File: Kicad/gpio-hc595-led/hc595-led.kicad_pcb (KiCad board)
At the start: 2 copper layers, 50 x 25 mm, 14 parts, among them K1 GPIO IN, K2 GPIO OUT, K3 DATA OUT, U1 74HC595, U2 3M-SJ5376

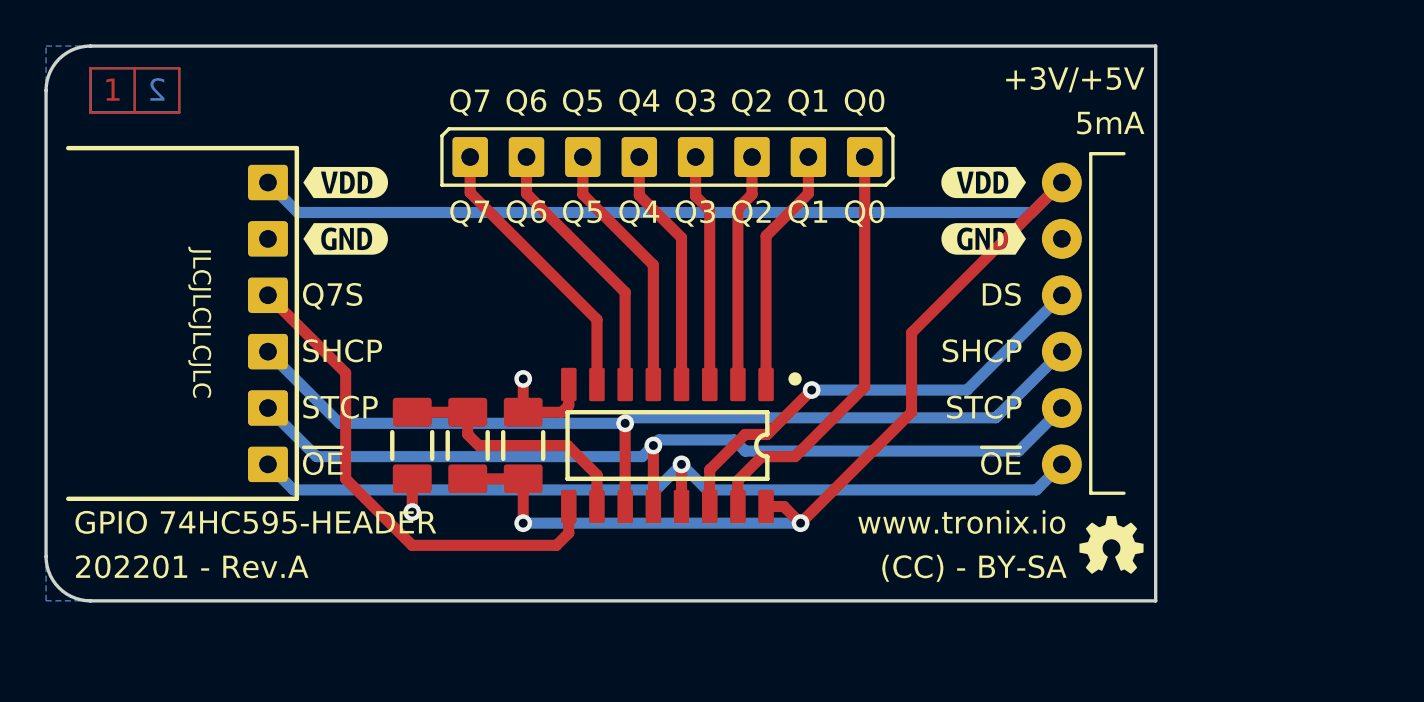
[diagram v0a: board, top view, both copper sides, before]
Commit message: GPIO HC595
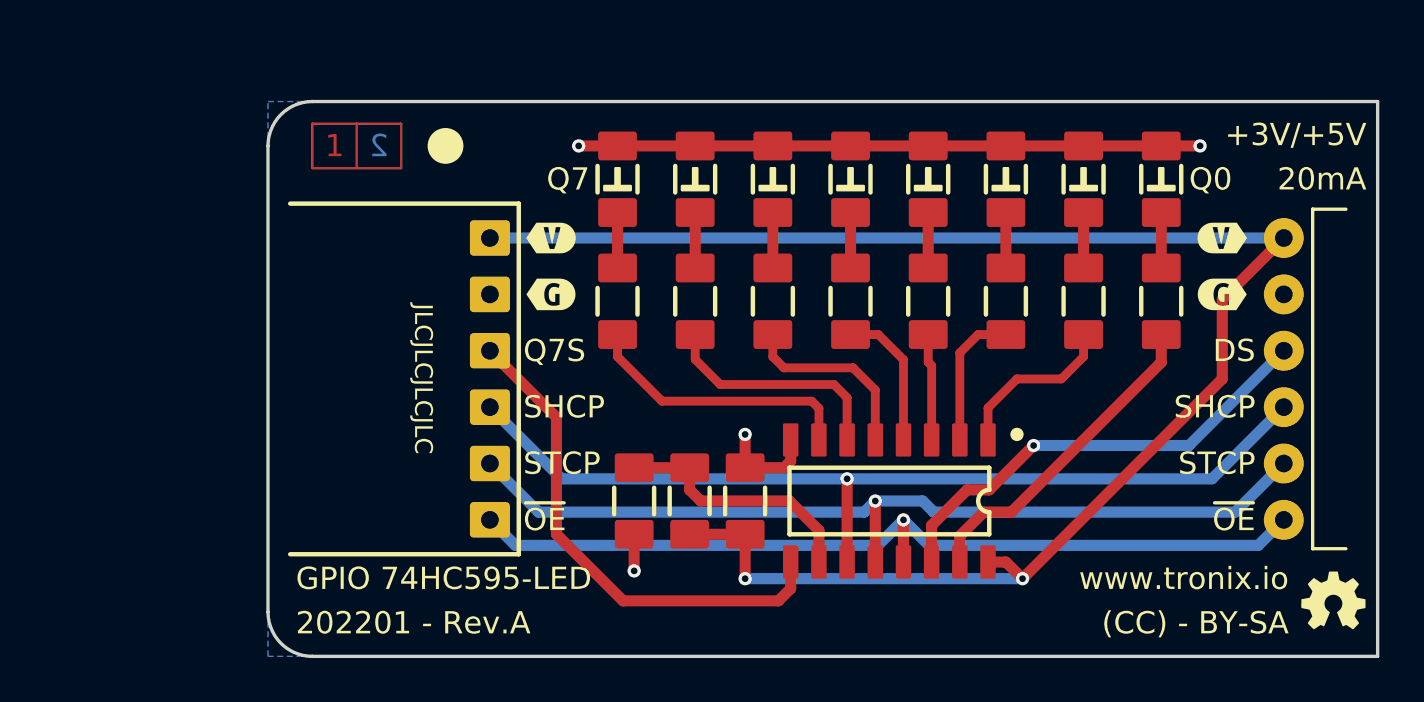
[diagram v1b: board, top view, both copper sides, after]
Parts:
- removed the C2 at (136.5, 90.5)
- removed K3: DATA OUT, tronixio:HARWIN-M20-999084x
- removed kibuzzard-62B2FE1A: G***, kibuzzard-62B2FE1A
- removed kibuzzard-62B2FE4D: G***, kibuzzard-62B2FE4D
- removed kibuzzard-62EAC0B7: G***, kibuzzard-62EAC0B7
- removed kibuzzard-62EAC0C0: G***, kibuzzard-62EAC0C0
- added C1: 10n, tronixio:CAPACITOR-SMD-1206, F.Cu at (141.5, 93.0)
- added LED1: D0, tronixio:LED-SMD-1206, F.Cu at (165.2, 78.5)
- added LED2: D1, tronixio:LED-SMD-1206, F.Cu at (161.8, 78.5)
- added LED3: D2, tronixio:LED-SMD-1206, F.Cu at (158.2, 78.5)
- added LED4: D3, tronixio:LED-SMD-1206, F.Cu at (154.8, 78.5)
- added LED5: D4, tronixio:LED-SMD-1206, F.Cu at (151.2, 78.5)
- added LED6: D5, tronixio:LED-SMD-1206, F.Cu at (147.8, 78.5)
- added LED7: D6, tronixio:LED-SMD-1206, F.Cu at (144.2, 78.5)
- added LED8: D7, tronixio:LED-SMD-1206, F.Cu at (140.8, 78.5)
- added R2: 4k7, tronixio:RESISTOR-SMD-1206, F.Cu at (140.8, 84.0)
- added R3: 4k7, tronixio:RESISTOR-SMD-1206, F.Cu at (144.2, 84.0)
- added R4: 4k7, tronixio:RESISTOR-SMD-1206, F.Cu at (147.8, 84.0)
- added R5: 4k7, tronixio:RESISTOR-SMD-1206, F.Cu at (151.2, 84.0)
- added R6: 4k7, tronixio:RESISTOR-SMD-1206, F.Cu at (154.8, 84.0)
- added R7: 4k7, tronixio:RESISTOR-SMD-1206, F.Cu at (158.2, 84.0)
- added R8: 4k7, tronixio:RESISTOR-SMD-1206, F.Cu at (161.8, 84.0)
- added R9: 4k7, tronixio:RESISTOR-SMD-1206, F.Cu at (165.2, 84.0)
- added kibuzzard-62B79DF9: G***, kibuzzard-62B79DF9, F.Cu at (137.8, 81.2)
- added kibuzzard-62B79E59: G***, kibuzzard-62B79E59, F.Cu at (137.8, 83.7)
- added kibuzzard-62B79EB2: G***, kibuzzard-62B79EB2, F.Cu at (168.0, 81.2)
- added kibuzzard-62B79EC3: G***, kibuzzard-62B79EC3, F.Cu at (168.0, 83.7)
- C2: renamed from C1; value 10n -> 100n
- R1: value 10K -> 10k
- moved C2 15.2 mm to (146.5, 93.0), turned to 90 degrees
- moved G*** 10.3 mm to (173.0, 97.5)
- moved K1 10.3 mm to (170.8, 81.2)
- moved K2 10.3 mm to (135.0, 93.8)
- moved R1 10.3 mm to (144.0, 93.0)
- moved U1 10.3 mm to (153.0, 93.0)
- moved U2 10.3 mm to (141.5, 87.5)
- moved GT 10.0 mm to (157.0, 81.5)
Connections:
- net POWER-GND renamed GND
- C2 pad 1: Net-(U1-~{MR}) -> +VDD
- K1 pad 1: POWER-VBAT -> +VDD
- K2 pad 6: POWER-VBAT -> +VDD
- R1 pad 1: POWER-VBAT -> +VDD
- U1 pad 16: POWER-VBAT -> +VDD
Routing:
- net POWER-VBAT: track 76.0 -> 0.00 mm, vias 2 -> 0
- net +VDD: track 0.00 -> 74.9 mm, vias 0 -> 2
- net GND: track 6.13 -> 34.3 mm, vias 2 -> 4
- net Net-(U1-Q3): track 10.5 -> 4.81 mm
- net Net-(U1-Q4): track 11.0 -> 6.47 mm
- net Net-(U1-Q0): track 19.0 -> 14.7 mm
- net Net-(U1-Q2): track 10.5 -> 6.34 mm
- net Net-(U1-Q1): track 11.0 -> 7.70 mm
- net Net-(U1-Q5): track 11.6 -> 8.49 mm
- net Net-(LED8-A): track 0.00 -> 2.50 mm
- net Net-(LED7-A): track 0.00 -> 2.50 mm
- net Net-(LED6-A): track 0.00 -> 2.50 mm
- net Net-(LED5-A): track 0.00 -> 2.50 mm
- net Net-(LED4-A): track 0.00 -> 2.50 mm
- net Net-(LED3-A): track 0.00 -> 2.50 mm
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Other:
- board text added: "20mA"
- board text added: "GPIO - 74HC595-LED - Rev.A - (01/2022) - Scale 100%"
- board text added: "GPIO 74HC595-LED"
- board text removed: "5mA"
- board text removed: "GPIO - 74HC595-HEADER - Rev.A - (01/2022) - Scale 100%"
- board text removed: "GPIO 74HC595-HEADER"
- board text removed: "Q1"
- board text removed: "Q2"
- board text removed: "Q3"
- board text removed: "Q4"
- board text removed: "Q5"
- board text removed: "Q6"
